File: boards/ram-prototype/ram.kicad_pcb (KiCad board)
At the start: 4 copper layers, 165 x 131 mm, 611 parts, among them J1 PinHeader_1x24_P2.54mm_Vertic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, J2 PinHeader_1x04_P2.54mm_Vertic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, J3 PinHeader_1x14_P2.54mm_Vertic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, J4 PinHeader_1x16_P2.54mm_Vertic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, U1 DSBGA\-5_NumericPads, U10 DSBGA\-5_NumericPads, U100 DSBGA\-5_NumericPads, U101 DSBGA\-5_NumericPads, U102 DSBGA\-5_NumericPads, U103 DSBGA\-5_NumericPads, U104 DSBGA\-5_NumericPads, U105 DSBGA\-5_NumericPads, U106 DSBGA\-5_NumericPads, U107 DSBGA\-5_NumericPads, U108 DSBGA\-5_NumericPads, U109 DSBGA\-5_NumericPads, U11 DSBGA\-5_NumericPads, U110 DSBGA\-5_NumericPads, U111 DSBGA\-5_NumericPads, U112 DSBGA\-5_NumericPads, U113 DSBGA\-5_NumericPads, U114 DSBGA\-5_NumericPads, U115 DSBGA\-5_NumericPads, U116 DSBGA\-5_NumericPads, U117 DSBGA\-5_NumericPads, U118 DSBGA\-5_NumericPads, U119 DSBGA\-5_NumericPads, U12 DSBGA\-5_NumericPads, U120 DSBGA\-5_NumericPads, U121 DSBGA\-5_NumericPads, U122 DSBGA\-5_NumericPads, U123 DSBGA\-5_NumericPads, U124 DSBGA\-5_NumericPads, U125 DSBGA\-5_NumericPads, U126 DSBGA\-5_NumericPads, U127 DSBGA\-5_NumericPads, U128 DSBGA\-5_NumericPads, U129 DSBGA\-5_NumericPads, U13 DSBGA\-5_NumericPads, U130 DSBGA\-5_NumericPads, U131 DSBGA\-5_NumericPads, U132 DSBGA\-5_NumericPads, U133 DSBGA\-5_NumericPads, U134 DSBGA\-5_NumericPads, U135 DSBGA\-5_NumericPads, U136 DSBGA\-5_NumericPads, U137 DSBGA\-5_NumericPads, U138 DSBGA\-5_NumericPads, U139 DSBGA\-5_NumericPads, U14 DSBGA\-5_NumericPads, U140 DSBGA\-5_NumericPads, U141 DSBGA\-5_NumericPads, U142 DSBGA\-5_NumericPads, U143 DSBGA\-5_NumericPads, U144 DSBGA\-5_NumericPads, U145 DSBGA\-5_NumericPads, U146 DSBGA\-5_NumericPads, U147 DSBGA\-5_NumericPads, U148 DSBGA\-5_NumericPads, U149 DSBGA\-5_NumericPads, U15 DSBGA\-5_NumericPads, U150 DSBGA\-5_NumericPads, U151 DSBGA\-5_NumericPads, U152 DSBGA\-5_NumericPads, U153 DSBGA\-5_NumericPads, U154 DSBGA\-5_NumericPads, U155 DSBGA\-5_NumericPads, U156 DSBGA\-5_NumericPads, U157 DSBGA\-5_NumericPads, U158 DSBGA\-5_NumericPads, U159 DSBGA\-5_NumericPads, U16 DSBGA\-5_NumericPads, U160 DSBGA\-5_NumericPads, U161 DSBGA\-5_NumericPads, U162 DSBGA\-5_NumericPads, U163 DSBGA\-5_NumericPads, U164 DSBGA\-5_NumericPads, U165 DSBGA\-5_NumericPads, U166 DSBGA\-5_NumericPads, U167 DSBGA\-5_NumericPads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

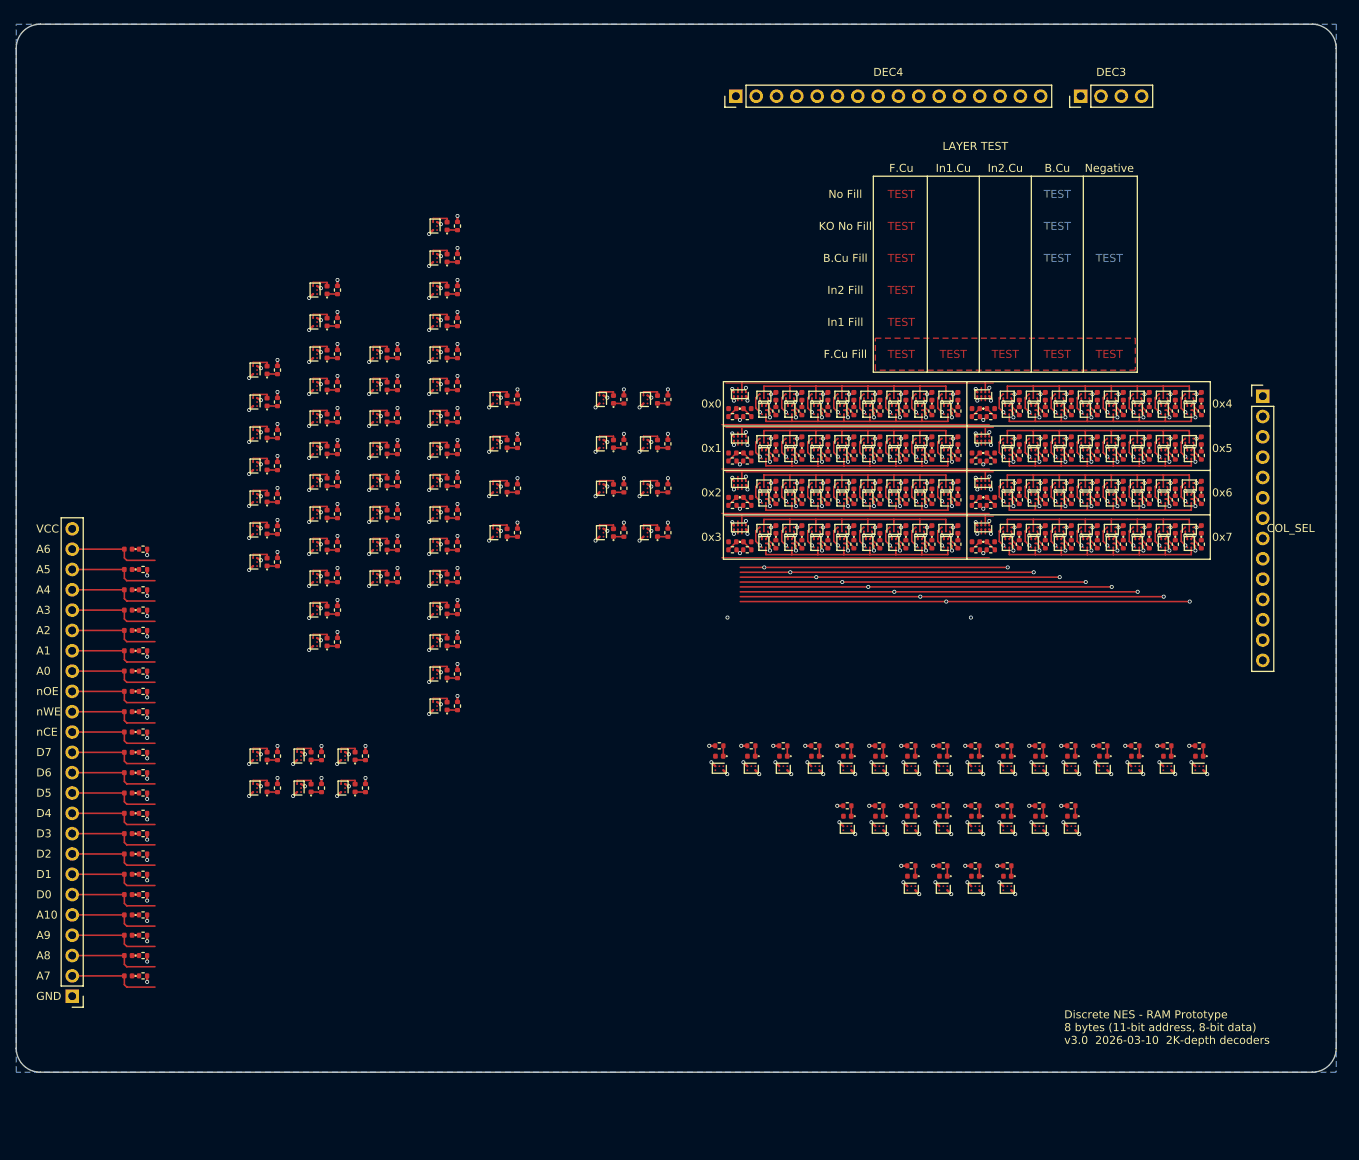
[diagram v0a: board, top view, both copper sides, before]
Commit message: R GND vias escape right, add IC→LED routing for rotated column_select
- Change R@90° GND via escape from UP (270°) to RIGHT (0°)
- Add 270° IC→LED 3-segment routing (LEFT-UP-RIGHT) for rotated
  column_select ICs — mirrors the 180° pattern rotated 90° CW
- Add 270° GND power via escape at 300° (up-right, d=0.55mm)
  to avoid new IC→LED traces
- IC→LED traces: 311 → 395 (+84 = 28 column_select ICs × 3 segs)

Default DRC: 0 errors, 0 warnings.

Co-Authored-By: Claude Opus 4.6 (1M context) <noreply@anthropic.com>
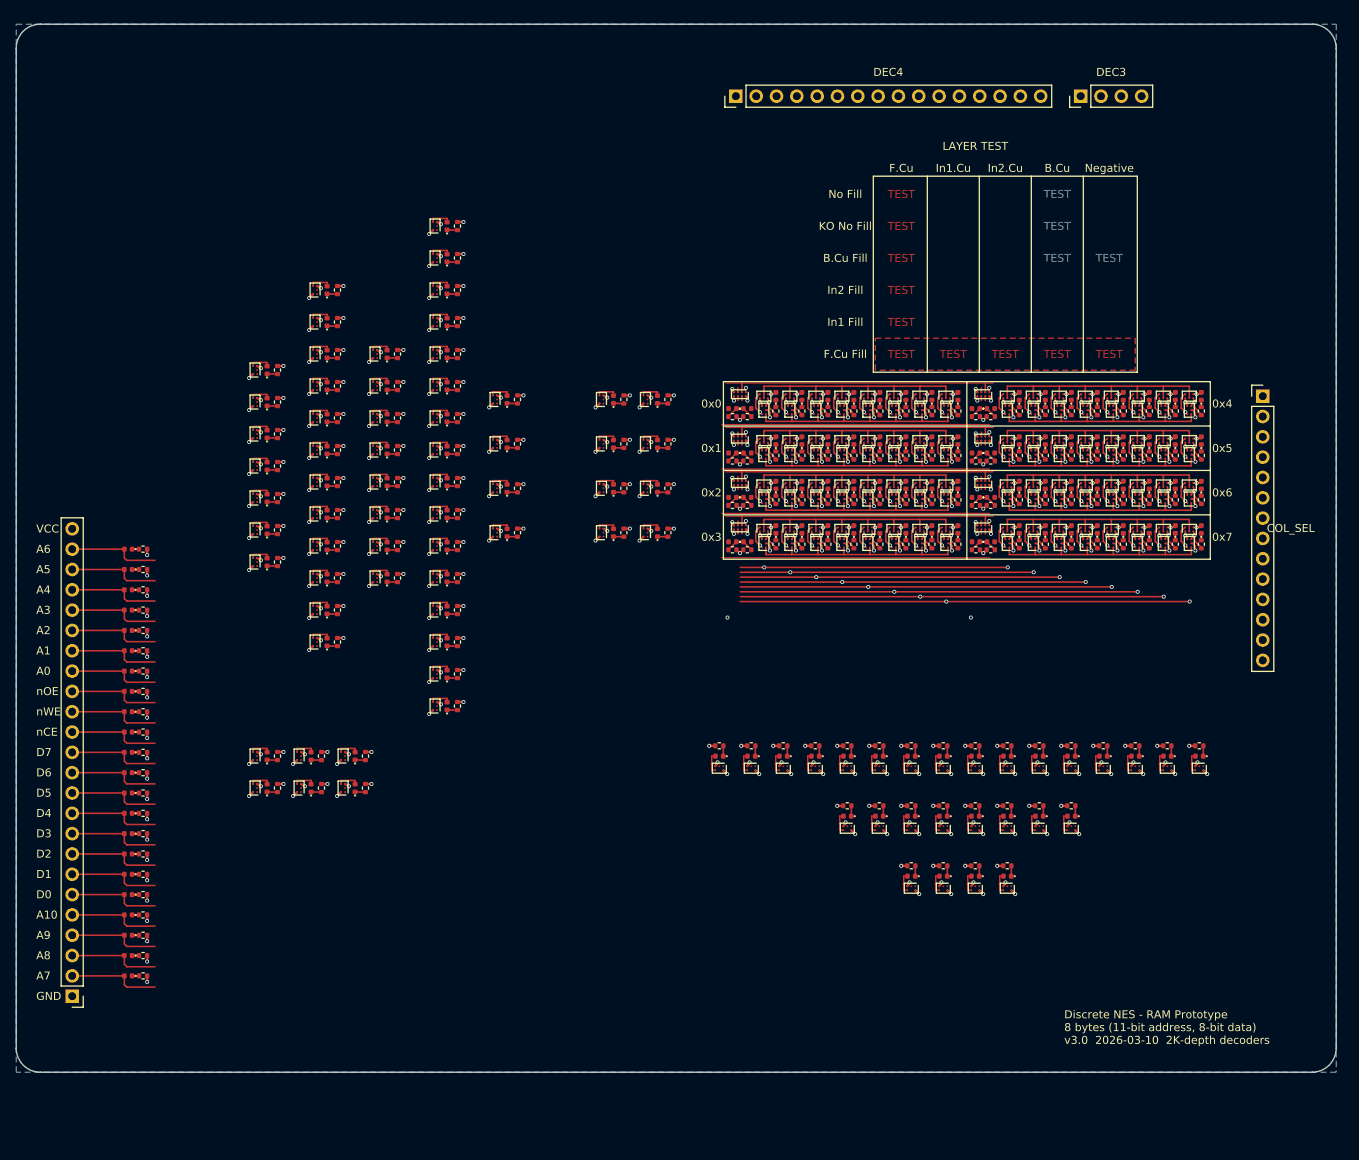
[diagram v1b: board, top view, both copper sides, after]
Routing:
- net GND: track 352.0 -> 348.1 mm
- net Net-(D70-A): track 0.00 -> 2.67 mm
- net /Column Select/GA2: track 0.00 -> 2.67 mm
- net /Column Select/GA1: track 0.00 -> 2.67 mm
- net /Column Select/GA0: track 0.00 -> 2.67 mm
- net /COL_SEL_6: track 0.00 -> 2.67 mm
- net /COL_SEL_5: track 0.00 -> 2.67 mm
- net /COL_SEL_4: track 0.00 -> 2.67 mm
- net /COL_SEL_3: track 0.00 -> 2.67 mm
- net /COL_SEL_2: track 0.00 -> 2.67 mm
- net /COL_SEL_1: track 43.6 -> 46.3 mm
- net /COL_SEL_0: track 43.6 -> 46.3 mm
- net Net-(D73-A): track 0.00 -> 2.66 mm
- net Net-(D72-A): track 0.00 -> 2.66 mm
- net Net-(D71-A): track 0.00 -> 2.66 mm
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
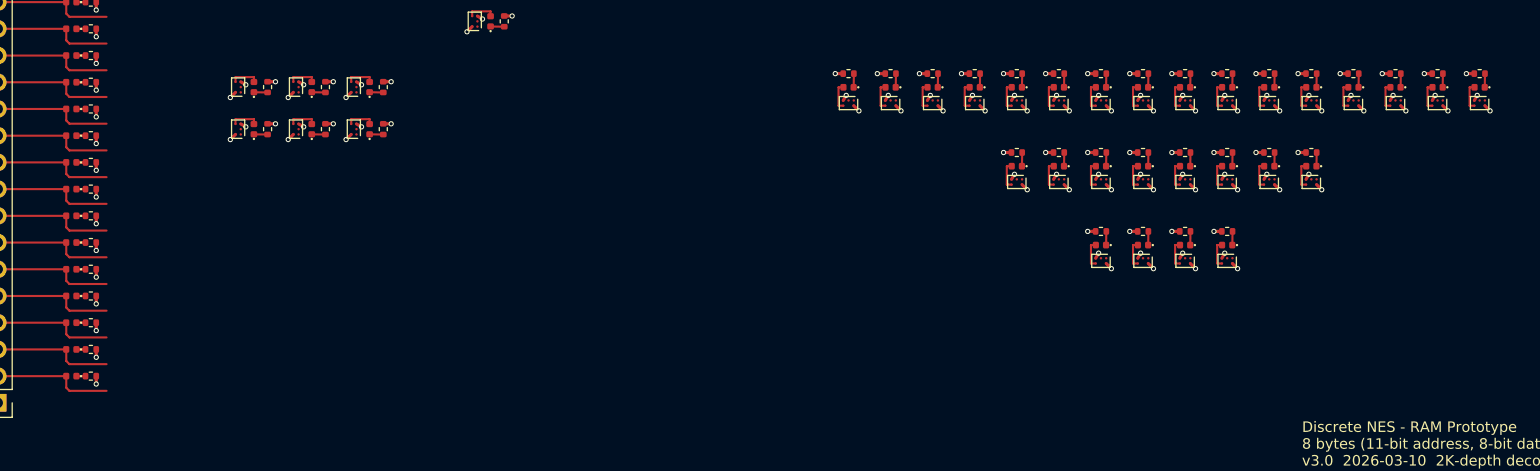
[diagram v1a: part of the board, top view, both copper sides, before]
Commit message: R GND vias escape right/up, IC→LED for rotated column_select
- R@90° (decoder/ctrl): GND escape changed from UP to RIGHT
- R@180° (rotated col_select): GND escape changed from LEFT to UP
  (away from LED below)
- Add 270° IC→LED 3-segment routing (LEFT-UP-RIGHT) for rotated
  column_select ICs — mirrors the 180° UP-RIGHT-DOWN pattern
- Add 270° GND power via escape at 300° (up-right, d=0.55mm)
- Fix C_Small crash: filter non-connector parts from extra_root list
- IC→LED traces: 311 → 395 (+84 segments)

Default DRC: 0 errors, 0 warnings.

Co-Authored-By: Claude Opus 4.6 (1M context) <noreply@anthropic.com>
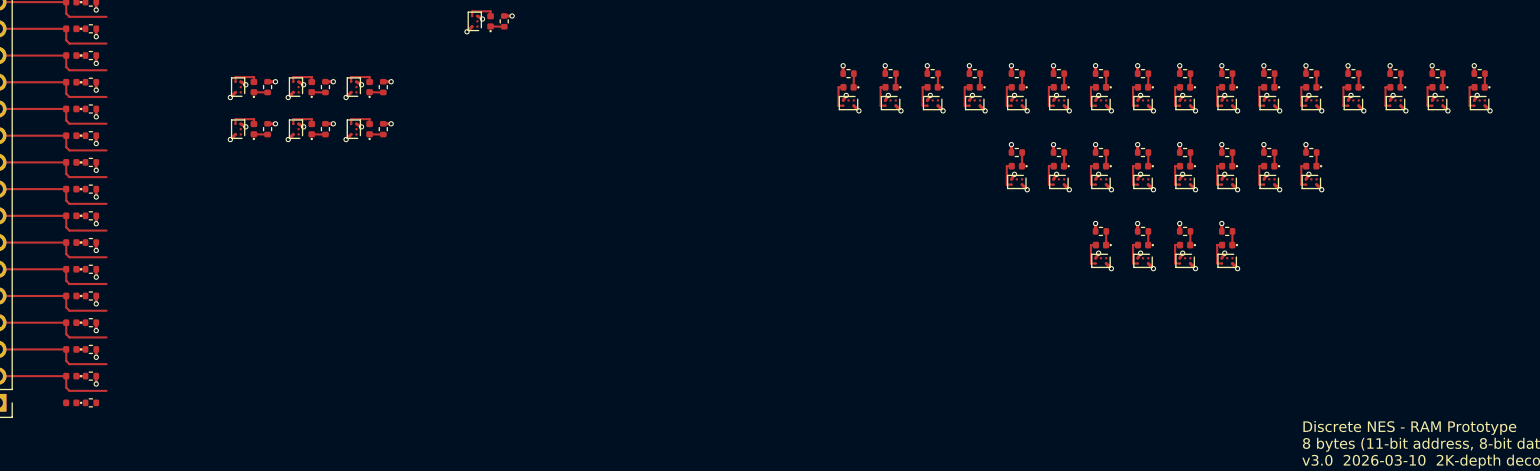
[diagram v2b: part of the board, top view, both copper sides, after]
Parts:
- added D192: LED_0402_1005Metric, LED_SMD:LED_0402_1005Metric, F.Cu at (27.0, 135.5)
- added R194: R_0402_1005Metric, Resistor_SMD:R_0402_1005Metric, F.Cu at (28.9, 135.5)

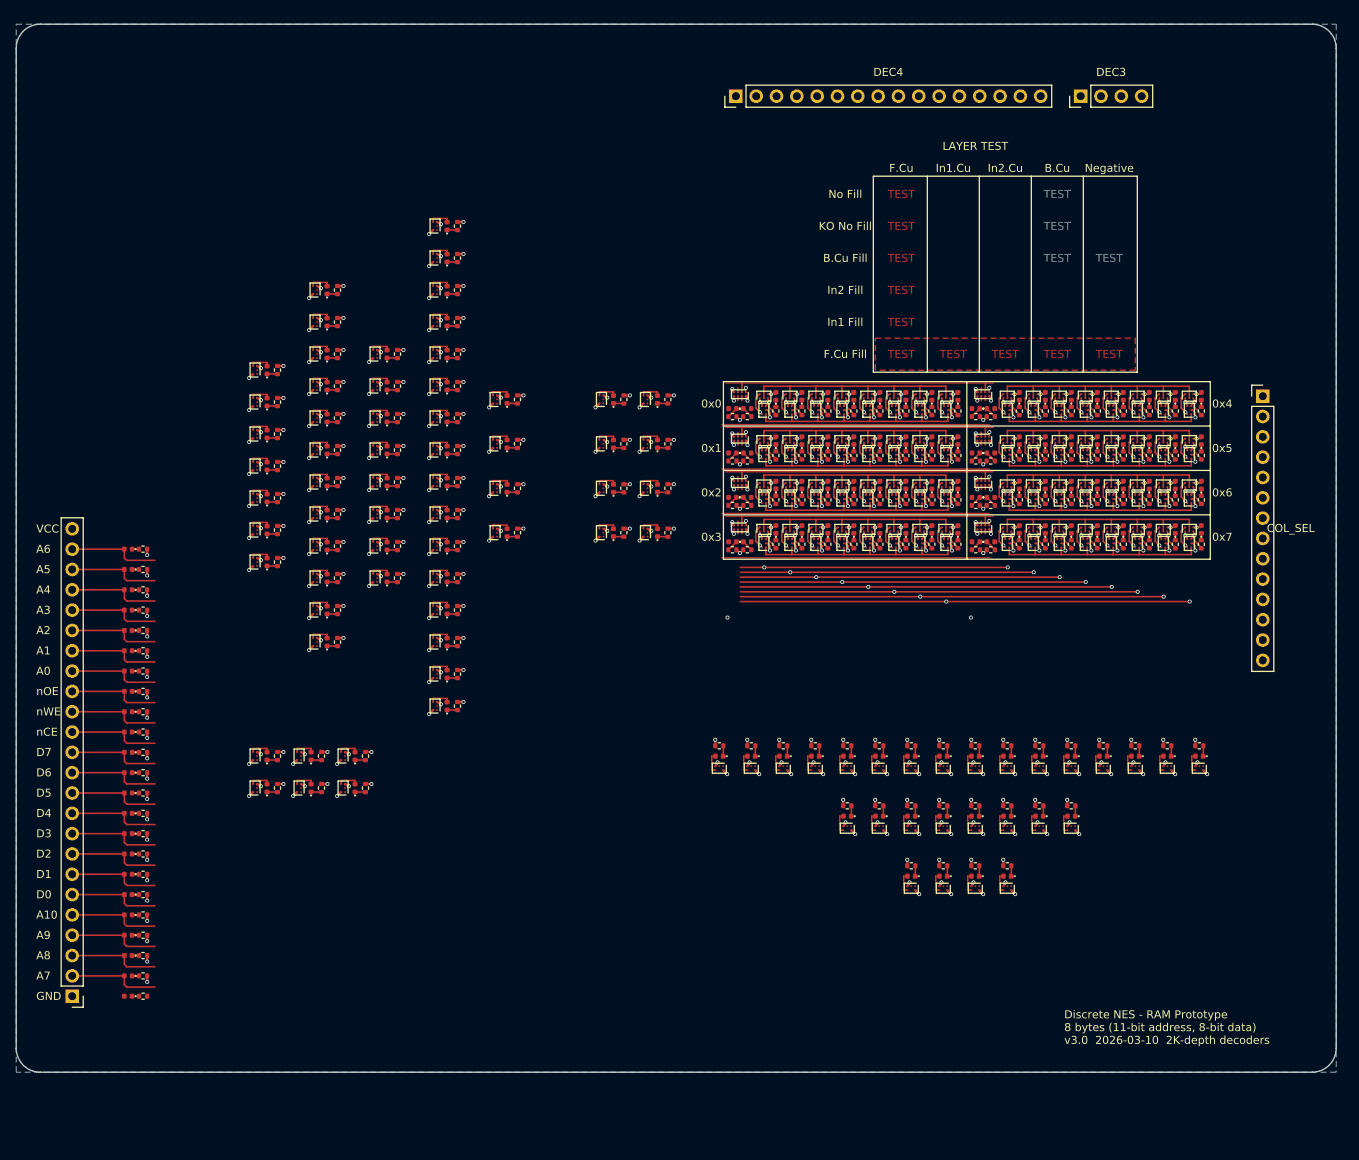
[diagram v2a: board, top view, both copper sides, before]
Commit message: add PCB layout for power supply section with custom TPS546D24A footprint
Places all 19 power supply components at the top-left corner of the
board, above the existing logic. Creates custom LQFN-CLIP-40 footprint
(5mm x 7mm, 0.5mm pitch) from TI RVF0040A datasheet land pattern.

Layout: Molex Mini-Fit Jr 2x4 (no mounting pegs) -> input caps ->
TPS546D24A with bypass caps tight against QFN -> inductor -> output
caps in 2 rows. PGOOD LED indicator below. All power components left
of RAM (8.5mm margin).

Changes:
- power_footprints.py: generates TPS546D24A_LQFN-CLIP-40 + SMD connector
- generate_pcb.py: power_supply group handling, fp_override for 0805 caps,
  Conn_02x support, 28mm Y shift for existing logic
- common.py: C_Small footprint, updated connector/IC mappings
- fp-lib-table: Power_Discrete library

Default DRC: 0 errors, 0 warnings.

Co-Authored-By: Claude Opus 4.6 (1M context) <noreply@anthropic.com>
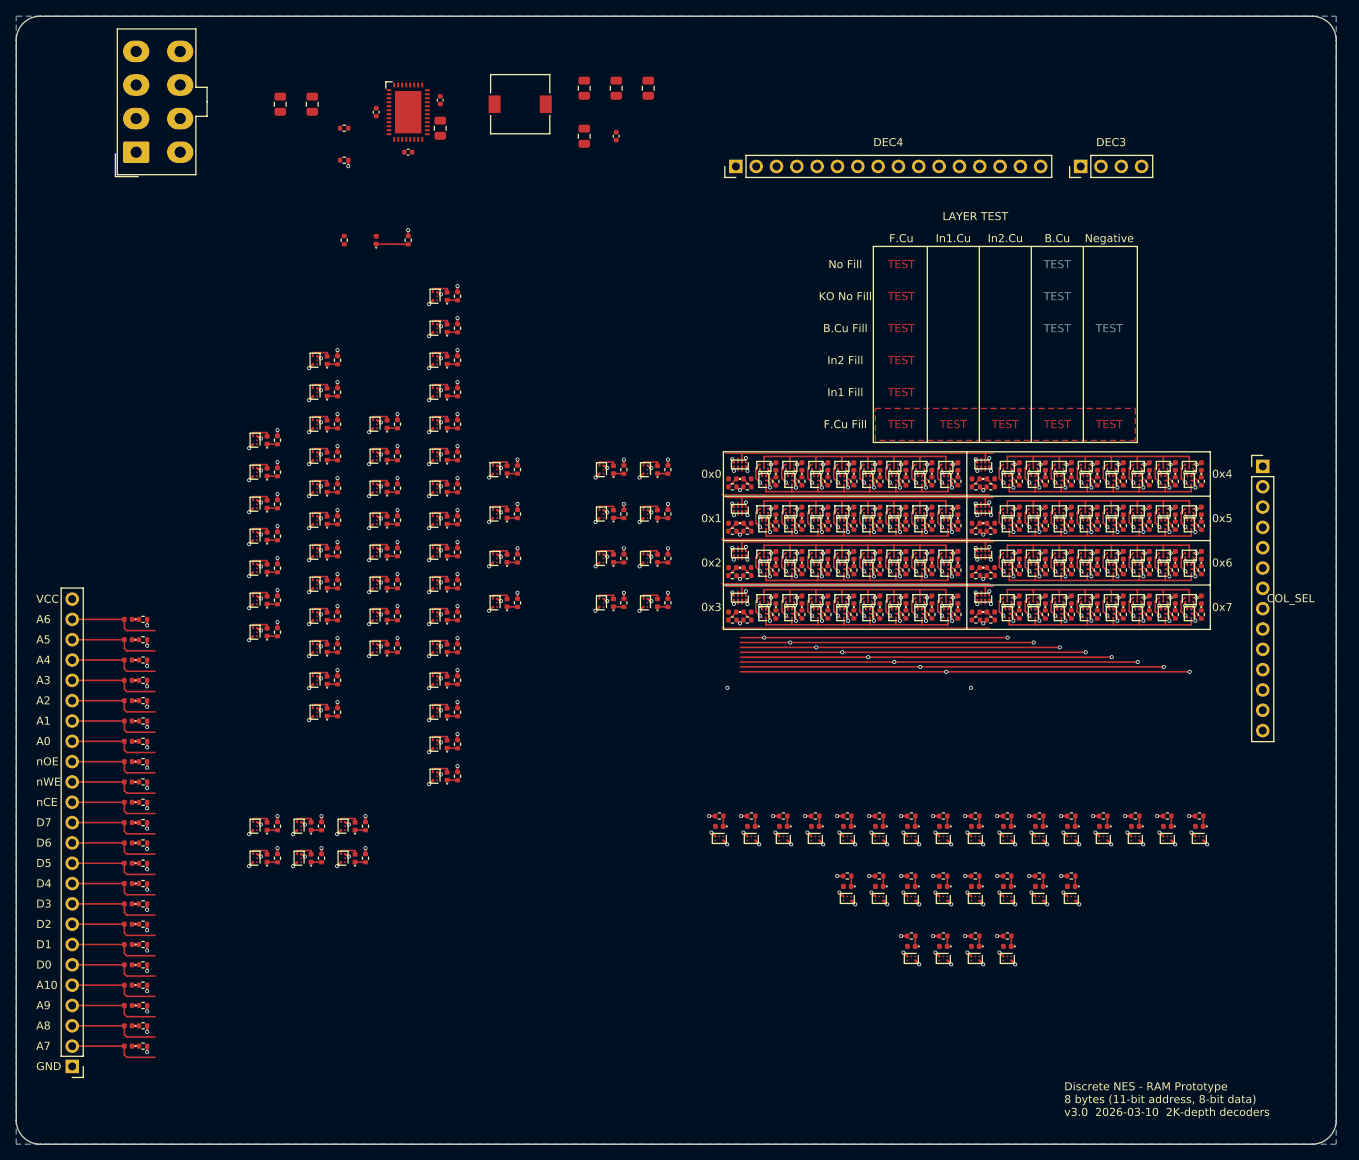
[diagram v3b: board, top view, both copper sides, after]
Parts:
- added C1: C_0805_2012Metric, Capacitor_SMD:C_0805_2012Metric, F.Cu at (46.0, 24.0)
- added C10: C_0805_2012Metric, Capacitor_SMD:C_0805_2012Metric, F.Cu at (84.0, 28.0)
- added C11: C_0402_1005Metric, Capacitor_SMD:C_0402_1005Metric, F.Cu at (88.0, 28.0)
- added C2: C_0805_2012Metric, Capacitor_SMD:C_0805_2012Metric, F.Cu at (50.0, 24.0)
- added C3: C_0402_1005Metric, Capacitor_SMD:C_0402_1005Metric, F.Cu at (58.0, 25.0)
- added C4: C_0402_1005Metric, Capacitor_SMD:C_0402_1005Metric, F.Cu at (66.0, 23.5)
- added C5: C_0805_2012Metric, Capacitor_SMD:C_0805_2012Metric, F.Cu at (66.0, 27.0)
- added C6: C_0402_1005Metric, Capacitor_SMD:C_0402_1005Metric, F.Cu at (62.0, 30.0)
- added C7: C_0805_2012Metric, Capacitor_SMD:C_0805_2012Metric, F.Cu at (84.0, 22.0)
- added C8: C_0805_2012Metric, Capacitor_SMD:C_0805_2012Metric, F.Cu at (88.0, 22.0)
- added C9: C_0805_2012Metric, Capacitor_SMD:C_0805_2012Metric, F.Cu at (92.0, 22.0)
- added J5: Molex_Mini-Fit_Jr_5566-08A_2x04_P4.20mm_Vertical, Connector_Molex:Molex_Mini-Fit_Jr_5566-08A_2x04_P4.20mm_Vertical, F.Cu at (28.0, 30.0)
- added L1: L_7.3x7.3_H4.5, Inductor_SMD:L_7.3x7.3_H4.5, F.Cu at (76.0, 24.0)
- added R192: R_0402_1005Metric, Resistor_SMD:R_0402_1005Metric, F.Cu at (54.0, 27.0)
- added R193: R_0402_1005Metric, Resistor_SMD:R_0402_1005Metric, F.Cu at (54.0, 31.0)
- added R195: R_0402_1005Metric, Resistor_SMD:R_0402_1005Metric, F.Cu at (62.0, 41.0)
- added U226: TPS546D24A, Power_Discrete:TPS546D24A_LQFN-CLIP-40, F.Cu at (62.0, 25.0)
- moved D192 99.5 mm to (58.0, 41.0), turned to 90 degrees
- moved R194 97.8 mm to (54.0, 41.0), turned to 90 degrees
- moved D18 8.78 mm to (27.0, 131.6)
- moved R18 8.78 mm to (28.9, 131.6)
- moved D1 8.78 mm to (27.0, 88.4)
- moved D10 8.78 mm to (27.0, 111.3)
- moved D11 8.78 mm to (27.0, 113.8)
- moved D112 8.78 mm to (104.4, 70.8)
- moved D113 8.78 mm to (104.4, 76.4)
- moved D114 8.78 mm to (104.4, 81.9)
- moved D115 8.78 mm to (104.4, 87.5)
- moved D116 8.78 mm to (134.8, 70.8)
- moved D117 8.78 mm to (134.8, 76.4)
- moved D118 8.78 mm to (134.8, 81.9)
- moved D119 8.78 mm to (134.8, 87.5)
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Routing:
- net GND: track 348.1 -> 353.6 mm, vias 280 -> 282
- net Net-(D192-K): track 0.00 -> 4.00 mm
- net Net-(D70-A): track 2.67 -> 0.00 mm
- net /Column Select/GA2: track 2.67 -> 0.00 mm
- net /Column Select/GA1: track 2.67 -> 0.00 mm
- net /Column Select/GA0: track 2.67 -> 0.00 mm
- net /COL_SEL_6: track 2.67 -> 0.00 mm
- net /COL_SEL_5: track 2.67 -> 0.00 mm
- net /COL_SEL_4: track 2.67 -> 0.00 mm
- net /COL_SEL_3: track 2.67 -> 0.00 mm
- net /COL_SEL_2: track 2.67 -> 0.00 mm
- net /COL_SEL_1: track 46.3 -> 43.6 mm
- net /COL_SEL_0: track 46.3 -> 43.6 mm
- net Net-(D73-A): track 2.66 -> 0.00 mm
- net Net-(D72-A): track 2.66 -> 0.00 mm
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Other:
- board size 165 x 131 mm -> 165 x 141 mm
